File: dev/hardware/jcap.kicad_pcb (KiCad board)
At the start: 2 copper layers, 68 parts, among them J201 CPU PGMR, J202 GPU PGMR, J203 SPARE GPU HDR, J204 SPARE CPU HDR, J301 Barrel_Jack_MountingPin, J502 VGA OUT, J601 CONTROLS, SW201 CPU ~{RES}, SW202 GPU ~{RES}, SW203 DEBUG, SW601 TILT, U101 P8X32A-D40, U201 P8X32A-D40, U302 LF33_TO220, U401 24LC256, U402 24LC256, U601 74HC165, U602 74HC165, Y1 6.5MHz, Y201 6.5MHz

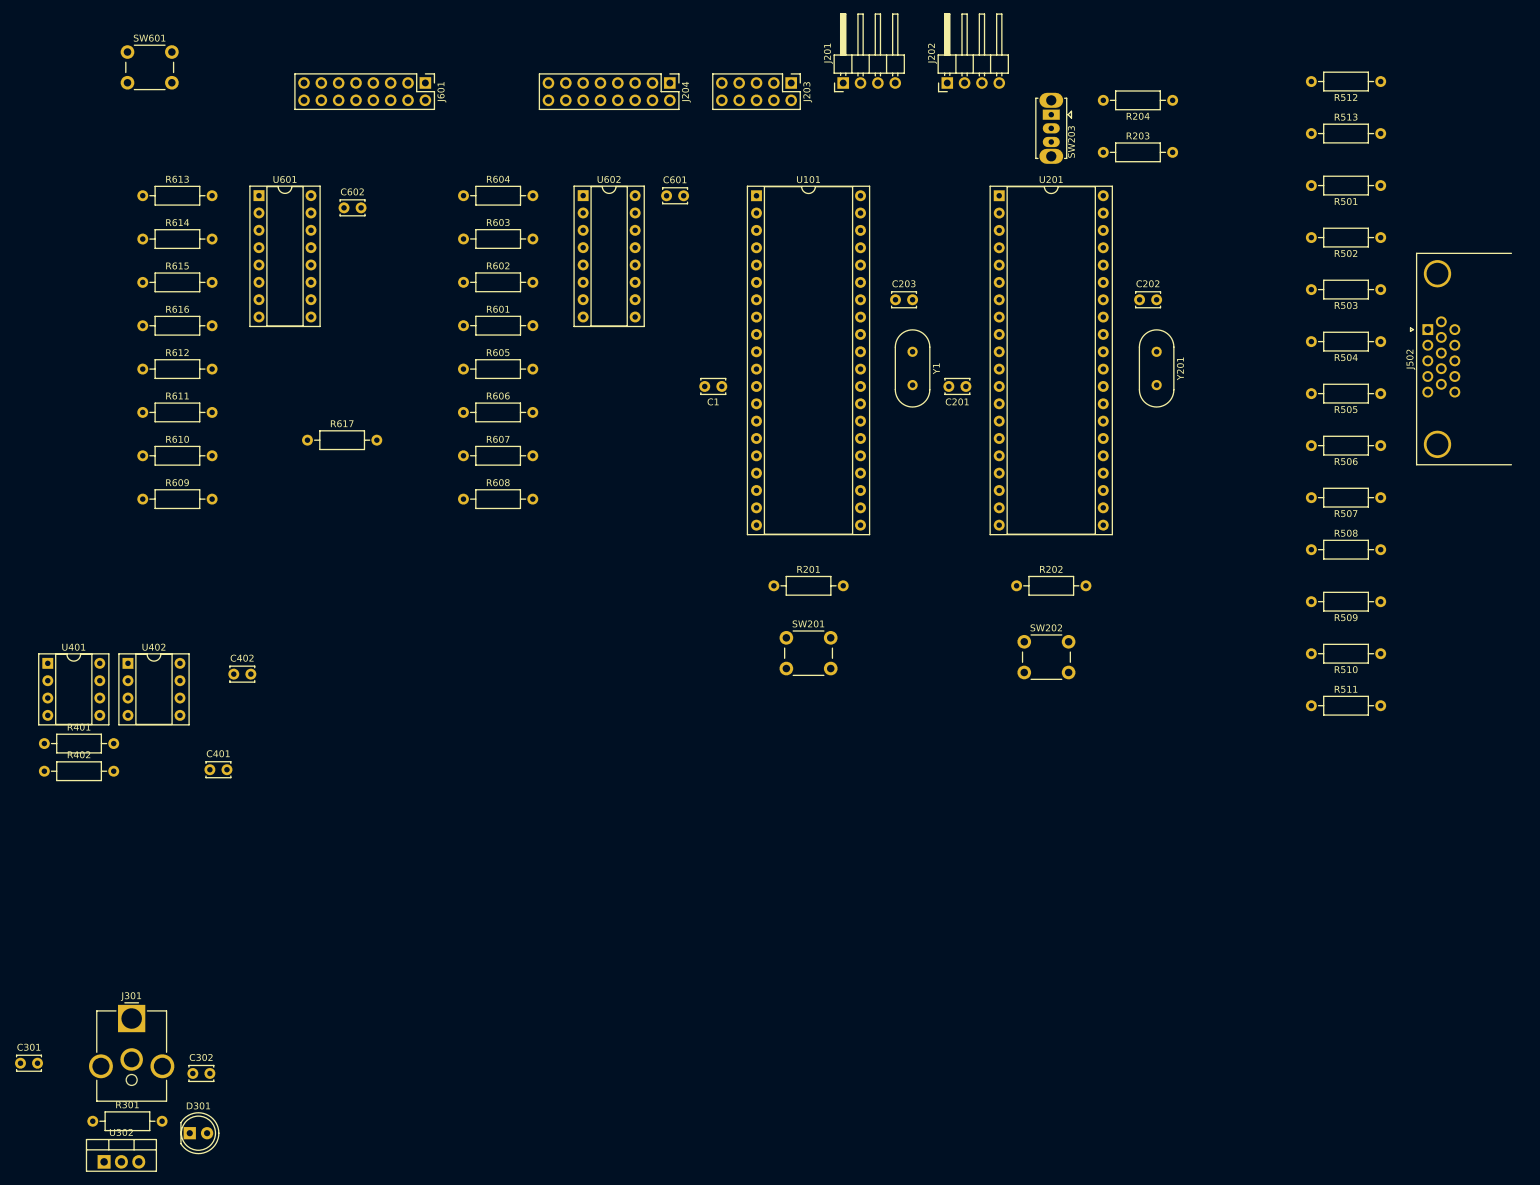
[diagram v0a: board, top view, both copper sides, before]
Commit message: Fixed resistors and reset PCB
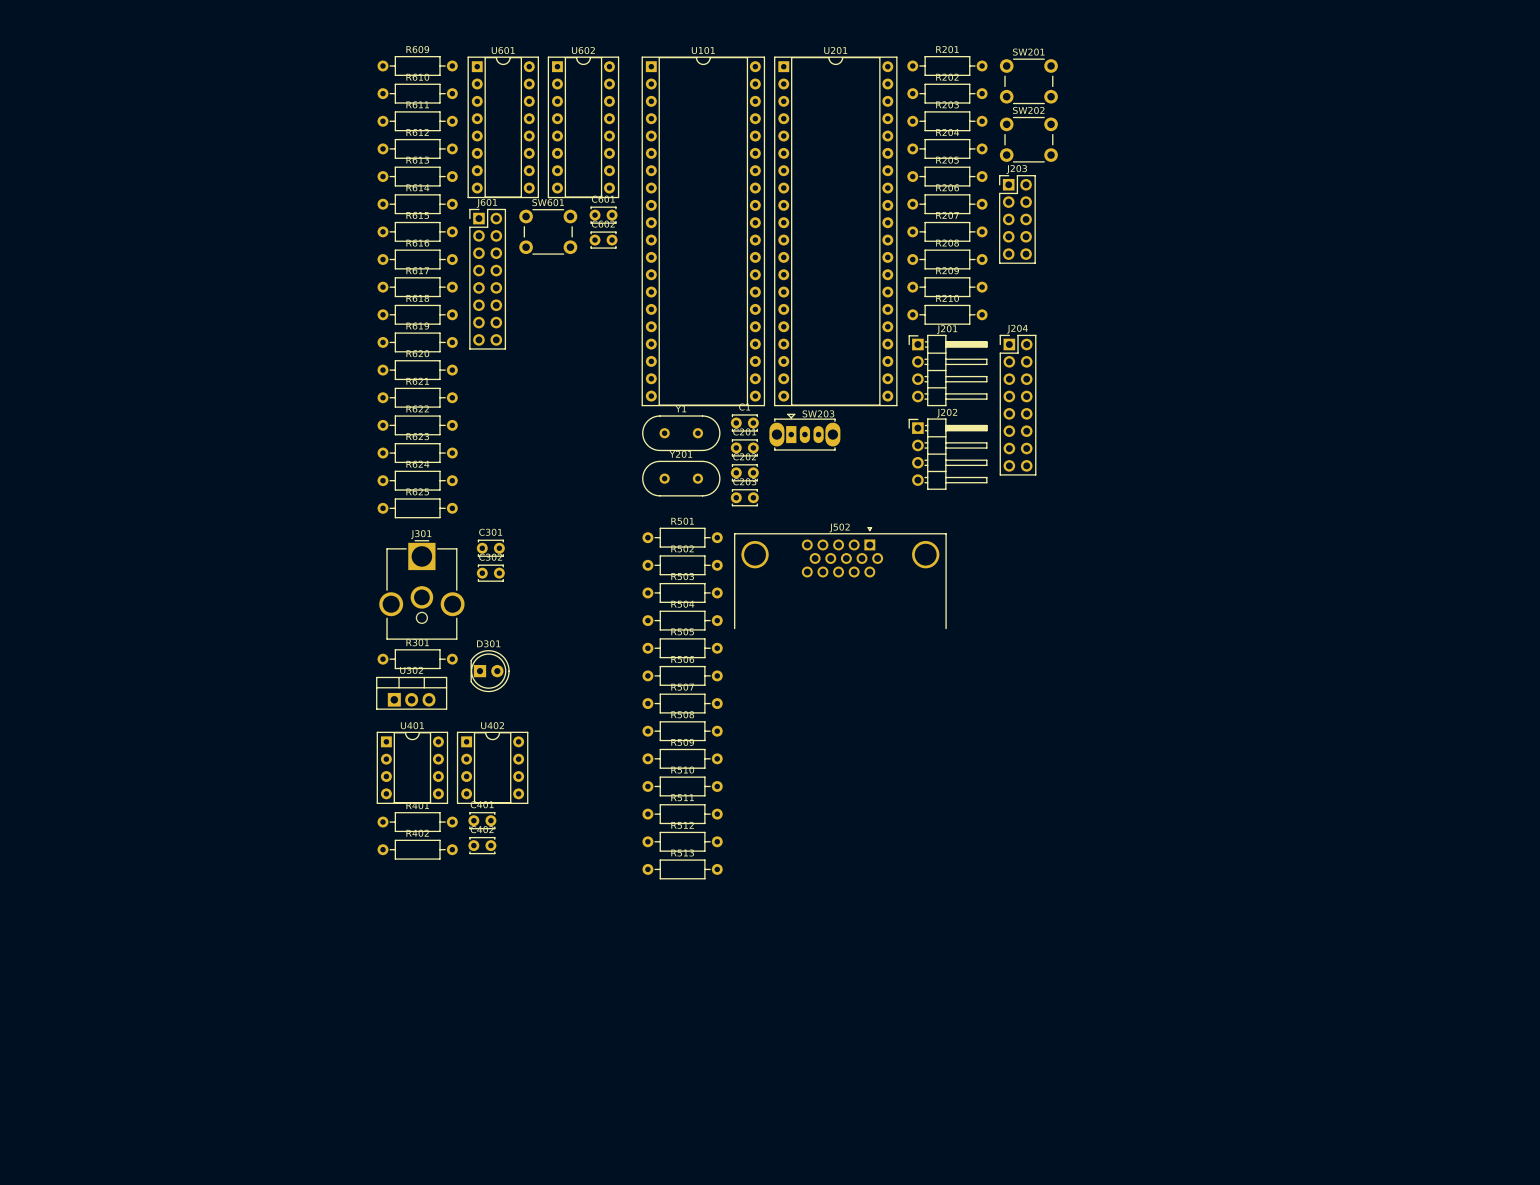
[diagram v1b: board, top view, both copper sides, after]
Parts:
- removed R601, R602, R603, R604, R605, R606, R607, R608: 10K, Resistor_THT:R_Axial_DIN0207_L6.3mm_D2.5mm_P10.16mm_Horizontal
- added R205: 200, Resistor_THT:R_Axial_DIN0207_L6.3mm_D2.5mm_P10.16mm_Horizontal, F.Cu at (155.0, 39.1)
- added R206: 200, Resistor_THT:R_Axial_DIN0207_L6.3mm_D2.5mm_P10.16mm_Horizontal, F.Cu at (155.0, 43.2)
- added R207: 200, Resistor_THT:R_Axial_DIN0207_L6.3mm_D2.5mm_P10.16mm_Horizontal, F.Cu at (155.0, 47.2)
- added R208: 200, Resistor_THT:R_Axial_DIN0207_L6.3mm_D2.5mm_P10.16mm_Horizontal, F.Cu at (155.0, 51.3)
- added R209: 200, Resistor_THT:R_Axial_DIN0207_L6.3mm_D2.5mm_P10.16mm_Horizontal, F.Cu at (155.0, 55.3)
- added R210: 200, Resistor_THT:R_Axial_DIN0207_L6.3mm_D2.5mm_P10.16mm_Horizontal, F.Cu at (155.0, 59.4)
- added R618: 10K, Resistor_THT:R_Axial_DIN0207_L6.3mm_D2.5mm_P10.16mm_Horizontal, F.Cu at (77.4, 59.4)
- added R619: 10K, Resistor_THT:R_Axial_DIN0207_L6.3mm_D2.5mm_P10.16mm_Horizontal, F.Cu at (77.4, 63.4)
- added R620: 10K, Resistor_THT:R_Axial_DIN0207_L6.3mm_D2.5mm_P10.16mm_Horizontal, F.Cu at (77.4, 67.5)
- added R621: 10K, Resistor_THT:R_Axial_DIN0207_L6.3mm_D2.5mm_P10.16mm_Horizontal, F.Cu at (77.4, 71.5)
- added R622: 10K, Resistor_THT:R_Axial_DIN0207_L6.3mm_D2.5mm_P10.16mm_Horizontal, F.Cu at (77.4, 75.6)
- added R623: 10K, Resistor_THT:R_Axial_DIN0207_L6.3mm_D2.5mm_P10.16mm_Horizontal, F.Cu at (77.4, 79.6)
- added R624: 10K, Resistor_THT:R_Axial_DIN0207_L6.3mm_D2.5mm_P10.16mm_Horizontal, F.Cu at (77.4, 83.7)
- added R625: 10K, Resistor_THT:R_Axial_DIN0207_L6.3mm_D2.5mm_P10.16mm_Horizontal, F.Cu at (77.4, 87.7)
- R201, R202, R203, R204: value 10K -> 200
- moved R512 154.7 mm to (116.2, 136.6), turned to 0 degrees
- moved R513 145.1 mm to (116.2, 140.6)
- moved R501 119.1 mm to (116.2, 92.0), turned to 0 degrees
- moved R502 117.6 mm to (116.2, 96.1), turned to 0 degrees
- moved R503 116.2 mm to (116.2, 100.1), turned to 0 degrees
- moved R504 114.9 mm to (116.2, 104.2), turned to 0 degrees
- moved R505 113.6 mm to (116.2, 108.2), turned to 0 degrees
- moved R506 112.5 mm to (116.2, 112.3), turned to 0 degrees
- moved R507 111.5 mm to (116.2, 116.3), turned to 0 degrees
- moved R509 109.8 mm to (116.2, 124.4), turned to 0 degrees
- moved R510 109.1 mm to (116.2, 128.5), turned to 0 degrees
- moved C301 101.3 mm to (91.9, 93.6)
- moved R508 100.8 mm to (116.2, 120.4)
- moved R511 98.5 mm to (116.2, 132.5)
- moved SW201 89.8 mm to (168.7, 22.9)
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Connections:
- J601 pad 1: Net-(J601-Pin_1) -> /Input/IN1
- J601 pad 10: Net-(J601-Pin_10) -> /Input/IN10
- J601 pad 11: Net-(J601-Pin_11) -> /Input/IN11
- J601 pad 12: Net-(J601-Pin_12) -> /Input/IN12
- J601 pad 13: Net-(J601-Pin_13) -> /Input/IN13
- J601 pad 14: Net-(J601-Pin_14) -> /Input/IN14
- J601 pad 15: Net-(J601-Pin_15) -> /Input/IN15
- J601 pad 16: Net-(J601-Pin_16) -> /Input/IN16
- J601 pad 2: Net-(J601-Pin_2) -> /Input/IN2
- J601 pad 3: Net-(J601-Pin_3) -> /Input/IN3
- J601 pad 4: Net-(J601-Pin_4) -> /Input/IN4
- J601 pad 5: Net-(J601-Pin_5) -> /Input/IN5
- J601 pad 6: Net-(J601-Pin_6) -> /Input/IN6
- J601 pad 7: Net-(J601-Pin_7) -> /Input/IN7
- J601 pad 8: Net-(J601-Pin_8) -> /Input/IN8
- J601 pad 9: Net-(J601-Pin_9) -> /Input/IN9
- R201 pad 1: GND -> /Propellers/GPU_DAT_1
- R201 pad 2: Net-(R201-Pad2) -> /Propellers/CPU_DAT_1
- R202 pad 1: Net-(U201-~{BOE}) -> /Propellers/GPU_DAT_2
- R202 pad 2: Net-(R202-Pad2) -> /Propellers/CPU_DAT_2
- R609 pad 1: Net-(J601-Pin_9) -> /Input/IN9
- R609 pad 2: /Input/IN9 -> +3.3V
- R610 pad 1: Net-(J601-Pin_10) -> /Input/IN10
- R610 pad 2: /Input/IN10 -> +3.3V
- R611 pad 1: Net-(J601-Pin_11) -> /Input/IN11
- R611 pad 2: /Input/IN11 -> +3.3V
- R612 pad 1: Net-(J601-Pin_12) -> /Input/IN12
- R612 pad 2: /Input/IN12 -> +3.3V
- R613 pad 1: Net-(J601-Pin_13) -> /Input/IN13
- R613 pad 2: /Input/IN13 -> +3.3V
- R614 pad 1: Net-(J601-Pin_14) -> /Input/IN14
- R614 pad 2: /Input/IN14 -> +3.3V
- R615 pad 1: Net-(J601-Pin_15) -> /Input/IN15
- R615 pad 2: /Input/IN15 -> +3.3V
- R616 pad 1: Net-(J601-Pin_16) -> /Input/IN16
- R616 pad 2: /Input/IN16 -> +3.3V
- R617 pad 1: GND -> Net-(U601-DS)
- R617 pad 2: Net-(R617-Pad2) -> +3.3V
- SW201 pad 1: Net-(R201-Pad2) -> GND
- SW202 pad 1: Net-(R202-Pad2) -> GND
- SW601 pad 1: Net-(R617-Pad2) -> GND
- U101 pad 21: /Propellers/GFX_DAT_8 -> /Propellers/CPU_DAT_8
- U101 pad 22: /Propellers/GFX_DAT_7 -> /Propellers/CPU_DAT_7
- U101 pad 23: /Propellers/GFX_DAT_6 -> /Propellers/CPU_DAT_6
- U101 pad 24: /Propellers/GFX_DAT_5 -> /Propellers/CPU_DAT_5
- U101 pad 25: /Propellers/GFX_DAT_4 -> /Propellers/CPU_DAT_4
- U101 pad 26: /Propellers/GFX_DAT_3 -> /Propellers/CPU_DAT_3
- U101 pad 27: /Propellers/GFX_DAT_2 -> /Propellers/CPU_DAT_2
- U101 pad 28: /Propellers/GFX_DAT_1 -> /Propellers/CPU_DAT_1
- U201 pad 10: Net-(U201-~{BOE}) -> GND
- U201 pad 13: /Propellers/GFX_DAT_1 -> /Propellers/GPU_DAT_1
- U201 pad 14: /Propellers/GFX_DAT_2 -> /Propellers/GPU_DAT_2
- U201 pad 15: /Propellers/GFX_DAT_3 -> /Propellers/GPU_DAT_3
- U201 pad 16: /Propellers/GFX_DAT_4 -> /Propellers/GPU_DAT_4
- U201 pad 17: /Propellers/GFX_DAT_5 -> /Propellers/GPU_DAT_5
- U201 pad 18: /Propellers/GFX_DAT_6 -> /Propellers/GPU_DAT_6
- U201 pad 19: /Propellers/GFX_DAT_7 -> /Propellers/GPU_DAT_7
- U201 pad 20: /Propellers/GFX_DAT_8 -> /Propellers/GPU_DAT_8

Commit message: Updated netclasses and PCB specs
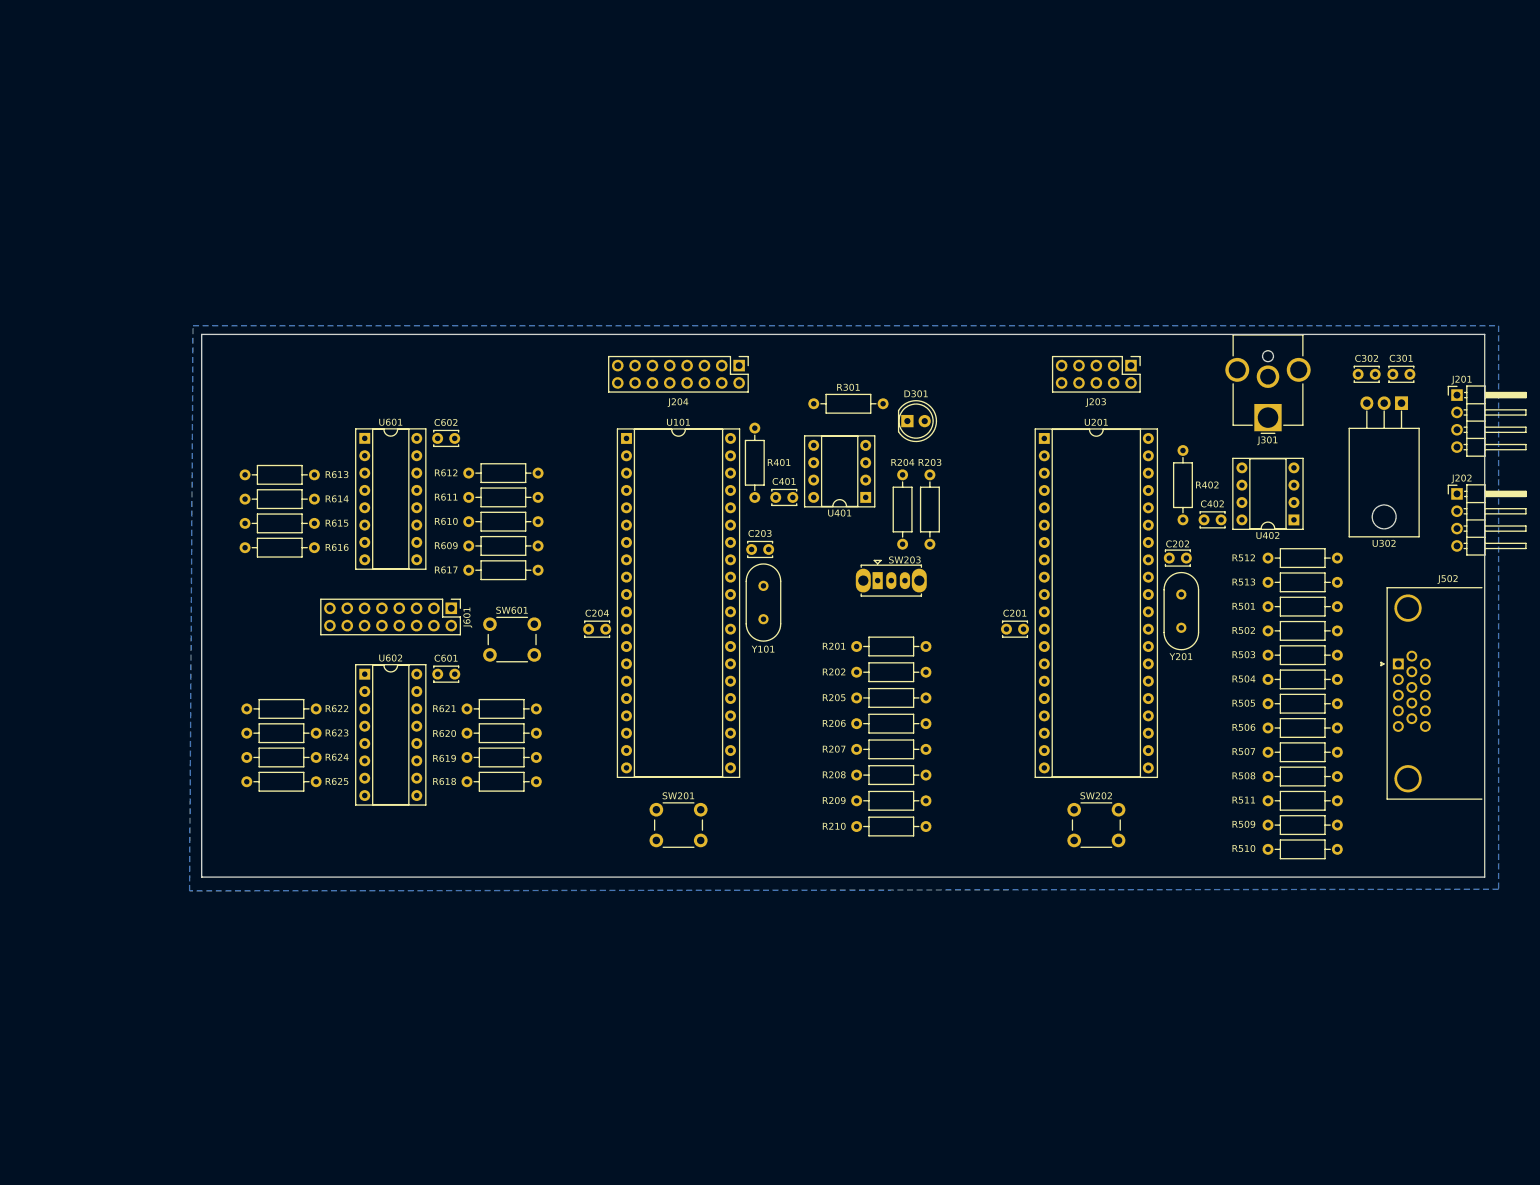
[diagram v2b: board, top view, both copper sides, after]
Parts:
- U302: footprint Package_TO_SOT_THT:TO-220-3_Vertical -> Package_TO_SOT_THT:TO-220-3_Horizontal_TabDown
- moved U302 153.8 mm to (226.6, 72.3), turned to 180 degrees
- moved C301 135.8 mm to (225.3, 68.1)
- moved C302 134.0 mm to (222.7, 68.1), turned to 180 degrees
- moved R402 131.0 mm to (194.6, 79.2), turned to -90 degrees
- moved J301 125.6 mm to (207.0, 74.4), turned to 180 degrees
- moved U402 125.5 mm to (210.8, 89.4), turned to 180 degrees
- moved SW201 120.4 mm to (117.4, 131.9)
- moved C402 117.1 mm to (197.6, 89.4)
- moved R512 109.2 mm to (217.2, 95.0), turned to 180 degrees
- moved R501 101.5 mm to (217.2, 102.1), turned to 180 degrees
- moved R509 101.5 mm to (217.2, 134.1), turned to 180 degrees
- moved R502 101.5 mm to (217.2, 105.7), turned to 180 degrees
- moved R510 101.4 mm to (217.2, 137.7), turned to 180 degrees
- moved R503 101.4 mm to (217.2, 109.2), turned to 180 degrees
- moved R504 101.4 mm to (217.2, 112.8), turned to 180 degrees
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- renumbered C1 to C204, Y1 to Y101
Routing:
- added copper zone on B.Cu, net GND
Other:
- board outline added: 188 x 79.5 mm
- rule pad_to_mask_clearance: 0 -> 0.0508

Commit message: Ready for routing
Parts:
- J301: value Barrel_Jack_MountingPin -> DC IN
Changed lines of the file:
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@@
         (effects (font (size 1 1) (thickness 0.15)))
     )
-    (fp_text value "Barrel_Jack_MountingPin" (at 0 13) (layer "F.Fab")
+    (fp_text value "DC IN" (at 0 13) (layer "F.Fab")
         (effects (font (size 1 1) (thickness 0.15)))
     )

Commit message: Finished draft PCB
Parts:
- J203: footprint Connector_PinHeader_2.54mm:PinHeader_2x05_P2.54mm_Vertical -> Connector_PinHeader_2.54mm:PinHeader_2x04_P2.54mm_Vertical
- J204: footprint Connector_PinHeader_2.54mm:PinHeader_2x08_P2.54mm_Vertical -> Connector_PinHeader_2.54mm:PinHeader_2x07_P2.54mm_Vertical
- moved R301 75.7 mm to (215.6, 81.5)
- moved J201 74.1 mm to (160.8, 76.5), turned to 90 degrees
- moved D301 65.3 mm to (219.5, 76.5)
- moved R622 39.5 mm to (105.9, 126.7)
- moved R623 39.5 mm to (105.9, 130.3)
- moved R624 39.5 mm to (105.9, 133.9)
- moved R625 39.5 mm to (105.9, 137.4)
- moved R613 38.7 mm to (105.9, 79.8)
- moved R614 38.7 mm to (105.9, 83.3)
- moved R615 38.7 mm to (105.9, 86.9)
- moved R616 38.7 mm to (105.9, 90.4)
- moved C601 36.1 mm to (120.1, 121.7)
- moved U602 35.9 mm to (109.2, 121.7)
- moved C602 34.9 mm to (120.1, 74.7)
- moved U601 34.6 mm to (109.2, 74.7)
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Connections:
- J203 pad 8: /Propellers/GPU_SPARE_8 -> unconnected-(J203-Pin_8-Pad8)
- J204 pad 14: /Propellers/CPU_SPARE_14 -> unconnected-(J204-Pin_14-Pad14)
- U101 pad 13: /Propellers/CPU_SPARE_8 -> /Propellers/CPU_SPARE_6
- U101 pad 14: /Propellers/CPU_SPARE_9 -> /Propellers/CPU_SPARE_7
- U101 pad 15: /Propellers/CPU_SPARE_10 -> /Propellers/CPU_SPARE_8
- U101 pad 16: /Propellers/CPU_SPARE_11 -> /Propellers/CPU_SPARE_9
- U101 pad 17: /Propellers/CPU_SPARE_12 -> /Propellers/CPU_SPARE_10
- U101 pad 18: /Propellers/CPU_SPARE_13 -> /Propellers/CPU_SPARE_11
- U101 pad 19: /Propellers/CPU_SPARE_14 -> /Propellers/CPU_SPARE_12
- U101 pad 20: /Propellers/CPU_SPARE_15 -> /Propellers/CPU_SPARE_13
- U101 pad 33: /Propellers/CPU_SPARE_1 -> unconnected-(U101-P24-Pad33)
- U101 pad 34: /Propellers/CPU_SPARE_2 -> unconnected-(U101-P25-Pad34)
- U101 pad 4: /Propellers/CPU_SPARE_3 -> /Propellers/CPU_SPARE_1
- U101 pad 5: /Propellers/CPU_SPARE_4 -> /Propellers/CPU_SPARE_2
- U101 pad 6: /Propellers/CPU_SPARE_5 -> /Propellers/CPU_SPARE_3
- U101 pad 7: /Propellers/CPU_SPARE_6 -> /Propellers/CPU_SPARE_4
- U101 pad 8: /Propellers/CPU_SPARE_7 -> /Propellers/CPU_SPARE_5
- U201 pad 2: /Propellers/GPU_SPARE_3 -> /Propellers/GPU_SPARE_1
- U201 pad 3: /Propellers/GPU_SPARE_4 -> /Propellers/GPU_SPARE_2
- U201 pad 35: /Propellers/GPU_SPARE_1 -> unconnected-(U201-P26-Pad35)
- U201 pad 36: /Propellers/GPU_SPARE_2 -> unconnected-(U201-P27-Pad36)
- U201 pad 4: /Propellers/GPU_SPARE_5 -> /Propellers/GPU_SPARE_3
- U201 pad 5: /Propellers/GPU_SPARE_6 -> /Propellers/GPU_SPARE_4
- U201 pad 6: /Propellers/GPU_SPARE_7 -> /Propellers/GPU_SPARE_5
- U201 pad 7: /Propellers/GPU_SPARE_8 -> /Propellers/GPU_SPARE_6
- U201 pad 8: /Propellers/GPU_SPARE_9 -> /Propellers/GPU_SPARE_7
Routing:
- net +3.3V: track 0.00 -> 471.6 mm
- net INPUTS_CLK: track 0.00 -> 89.3 mm
- net ~{INPUTS_PL}: track 0.00 -> 88.0 mm
- net /Propellers/~{SER_RES_CPU}: track 0.00 -> 83.4 mm
- net /Propellers/~{SER_RES_GPU}: track 0.00 -> 83.3 mm
- net INPUTS: track 0.00 -> 66.9 mm
- net /Propellers/DEBUG: track 0.00 -> 63.1 mm
- net V_SYNC: track 0.00 -> 60.2 mm
- net /Input/IN8: track 0.00 -> 40.8 mm
- net Net-(J502-Pad14): track 0.00 -> 38.3 mm
- net /Input/IN7: track 0.00 -> 37.3 mm
- net /Input/IN12: track 0.00 -> 33.0 mm
- net Net-(J502-Pad13): track 0.00 -> 32.2 mm
- net /Input/IN10: track 0.00 -> 31.9 mm
- net /VGA_DAC/RED_OUT: track 0.00 -> 28.8 mm
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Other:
- board size 188 x 79.5 mm -> 149.1 x 77 mm
- board text added: "U302"
